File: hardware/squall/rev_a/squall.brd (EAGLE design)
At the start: 25.4 x 25.4 mm, 47 parts, among them IC1 FT232RQ, J1 MICRO_USB_B_HIROSE_ZX62R-B-5P, J2 TC2030-CTX-NL, J5 MICRO_USB_B_JST_MC5BR3-M404-4S, J6 HIROSE-DF40C-10DP-0.4V, J7 HIROSE-DF40C-10DP-0.4V, U1 FT232RL, U3 NRF51822QF, U4 LDK120PU30R, X2 16MHz

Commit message: updated squall
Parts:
- removed C1, C2, C4: 0.1u, rcl:C0603
- removed C5: 10u, SparkFun:EIA3216
- removed D2: BLUE, SparkFun:LED-0603
- removed D3: GREEN, SparkFun:LED-0603
- removed D4: RED, SparkFun:LED-0603
- removed J1: MICRO_USB_B_HIROSE_ZX62R-B-5P, connector:USB_MICRO_B-HIROSE-ZX62R-B-5P
- removed L1: (no value), SparkFun:0603
- removed R3, R4: 470, rcl:R0603
- removed U1: FT232RL, ftdichip:SSOP28
- R2: value 470 -> 12k; device rcl:R0603 -> passives:0402_RES
- moved R2 38.2 mm to (0.64, 12.7), turned to 90 degrees
- moved R8 8.91 mm to (19.1, 16.9)
- moved C18 4.64 mm to (5.21, 7.85), turned to 270 degrees
- moved C20 4.49 mm to (0.00, 19.1)
- moved U4 4.49 mm to (-0.03, 20.3)
- moved C17 4.44 mm to (11.9, 10.3), turned to 270 degrees
- moved C19 3.24 mm to (1.85, 21.8)
- moved L2 3.02 mm to (20.6, 17.6)
- moved J2 1.74 mm to (19.9, 7.09), turned to 315 degrees
- moved C3 1.51 mm to (19.8, 17.6), turned to 270 degrees
- moved L3 1.15 mm to (20.6, 15.4), turned to 270 degrees
- moved C7 0.93 mm to (17.7, 11.9)
- moved C12 0.80 mm to (17.9, 19.4)
- moved C16 0.63 mm to (13.7, 10.3)
- moved J7 0.63 mm to (3.17, 15.2), turned to 0 degrees
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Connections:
- net N$12 renamed AVDD
- net N$13 renamed DCC
- net N$28 renamed FTDI_VCC
- removed net !RST_USB: U1.3
- removed net MISO: U3.47
- removed net MOSI: U3.48
- removed net N$10: R2.1, U1.23
- removed net N$15: R3.1, U1.22
- removed net N$20: D2.C, R2.2
- removed net N$21: D3.C, R3.2
- removed net N$22: D4.C, R4.2
- removed net N$24: C16.1, J5.1, L4.1
- removed net N$25: C19.1, U4.4, U4.6
- removed net N$29: C18.1, IC1.1, IC1.16
- removed net N$8: J1.3, U1.15
- removed net N$9: C2.1, C5.A, L1.2, U1.20
- removed net RX: U1.1
- removed net SCK: U3.44
- removed net TX: U1.5
- removed net USB5V: C1.1, J1.1, L1.1
- new net 5V: C16.1, C19.1, J5.1, J7.10, J7.8, L4.1, U4.4, U4.6
- new net A5: J6.9, U3.8
- new net A6: J6.7, U3.9
- new net A7: J6.5, U3.10
- new net P08: J6.3, U3.14
- new net P09: J6.1, U3.15
- new net P10: J6.10, U3.16
- new net P11: J6.8, U3.17
- new net P12: J6.6, U3.18
- new net PROG_RX: IC1.30, U3.47
- new net PROG_TX: IC1.2, U3.48
- net 3V3: now also C18.1, IC1.1, IC1.16; no longer C4.1, D2.A, D3.A, D4.A, U1.17, U1.4
- net GND: now also BAT1.GND, J7.1, J7.9, U$2.NEG; no longer C1.2, C2.2, C4.2, C5.C, J1.5, R4.1, U1.18, U1.21, U1.25, U1.26, U1.7
- net N$1: now also R2.2, U$2.POS; no longer J1.2, U1.16
- net N$7: now also U3.19; no longer U3.15
- net SWDCLK: now also J6.2
- net SWDIO: now also J6.4
- net TCK: no longer U1.2
- net VCC: now also BAT1.POS1, BAT1.POS2, BAT1.POS3, BAT1.POS4, J7.2, J7.4, R2.1
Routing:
- net SWDCLK: track 0.00 -> 23.0 mm, vias 0 -> 2
- net SWDIO: track 0.00 -> 16.3 mm, vias 0 -> 2
- net 5V: track 0.00 -> 15.8 mm, vias 0 -> 1
- net 3V3: track 0.00 -> 12.0 mm, vias 0 -> 2
- net DCC: track 0.00 -> 11.9 mm, vias 0 -> 2
- net AVDD: track 0.00 -> 11.2 mm, vias 0 -> 2
- net P11: track 0.00 -> 10.0 mm
- net P12: track 0.00 -> 9.97 mm
- net PROG_TX: track 0.00 -> 9.70 mm, vias 0 -> 2
- net P10: track 0.00 -> 9.63 mm
- net A5: track 0.00 -> 8.33 mm
- net PROG_RX: track 0.00 -> 8.11 mm
- net N$16: track 0.00 -> 7.95 mm
- net A6: track 0.00 -> 7.87 mm
- net N$7: track 0.00 -> 7.09 mm, vias 0 -> 2
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
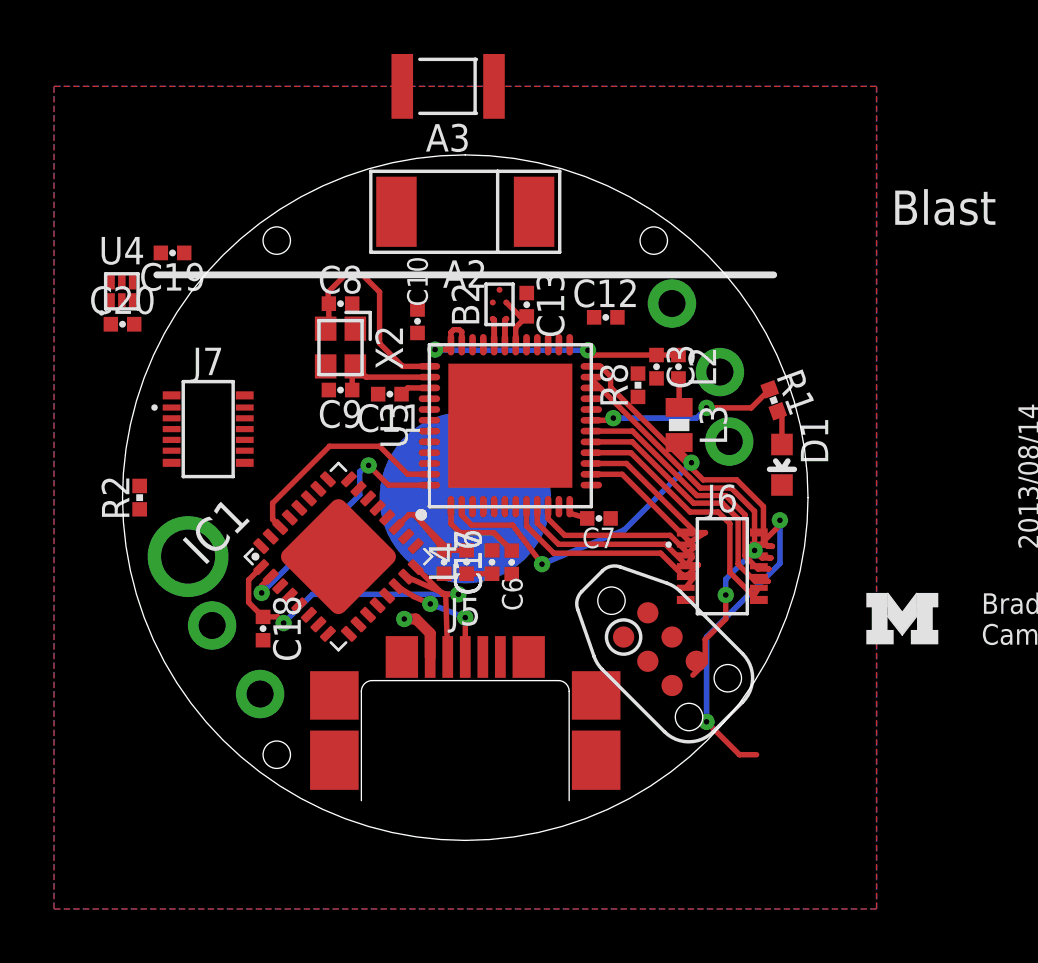
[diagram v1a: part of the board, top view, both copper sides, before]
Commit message: squall mostly routed
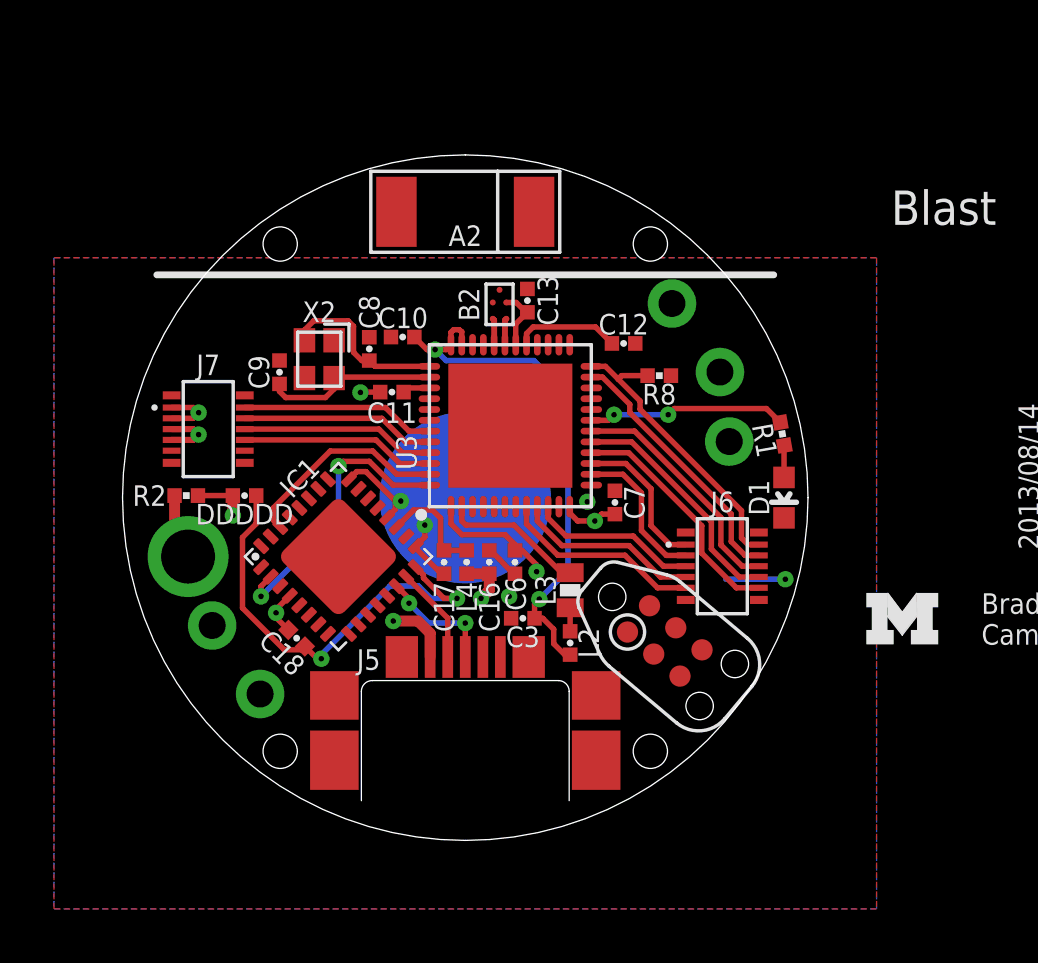
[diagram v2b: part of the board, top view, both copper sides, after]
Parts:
- removed A3: FRACTUS-2.4GHZ-FR05-S1-N-0-110, chips:FRACTUS-ANTENNA-FR05-S1-N-0-110
- removed C19, C20: 1uF, passives:0402_CAP
- removed U4: LDK120PU30R, chips:DFN6L-1.2MMX1.3MM
- added DDDDD: DIODE, passives:0402_CAP
- moved L2 11.0 mm to (16.6, 7.32), turned to 90 degrees
- moved C3 10.6 mm to (14.8, 8.23), turned to 180 degrees
- moved L3 7.33 mm to (16.6, 9.27), turned to 90 degrees
- moved C9 2.36 mm to (5.82, 17.3), turned to 90 degrees
- moved C8 1.99 mm to (9.14, 18.2), turned to 90 degrees
- moved R2 1.73 mm to (2.36, 12.8), turned to 180 degrees
- moved C18 1.29 mm to (6.45, 7.49), turned to 135 degrees
- moved R1 1.28 mm to (24.4, 15.1), turned to 280 degrees
- moved D1 1.22 mm to (24.5, 12.7)
- moved C12 1.17 mm to (18.6, 18.4)
- moved X2 0.90 mm to (7.29, 17.8)
- moved R8 0.86 mm to (19.9, 17.2), turned to 0 degrees
- moved C7 0.84 mm to (18.2, 12.5), turned to 90 degrees
- moved C10 0.80 mm to (10.4, 18.7), turned to 180 degrees
- moved J2 0.35 mm to (20.1, 7.39), turned to 320 degrees
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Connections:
- removed net N$31: C20.1, U4.1
- new net A0: J7.6, U3.45
- new net A1: J7.8, U3.46
- new net P24: J7.2, U3.43
- new net P25: J7.4, U3.44
- net 3V3: now also DDDDD.2
- net 5V: now also J7.5, J7.7; no longer C19.1, J7.10, J7.8, U4.4, U4.6
- net GND: now also J7.10; no longer C19.2, C20.2, J7.1, U4.2, U4.5
- net VCC: now also DDDDD.1, J7.1, J7.3; no longer J7.2, J7.4
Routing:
- net SWDCLK: track 23.0 -> 10.9 mm, vias 2 -> 0
- net GND: track 0.00 -> 9.39 mm, vias 0 -> 6
- net AVDD: track 11.2 -> 19.7 mm
- net P25: track 0.00 -> 7.20 mm
- net A1: track 0.00 -> 7.20 mm
- net A0: track 0.00 -> 7.20 mm
- net P24: track 0.00 -> 7.20 mm
- net VCC: track 4.21 -> 11.2 mm, vias 0 -> 4
- net DCC: track 11.9 -> 5.34 mm, vias 2 -> 0
- net 5V: track 15.8 -> 22.1 mm, vias 1 -> 3
- net 3V3: track 12.0 -> 16.7 mm
- net SWDIO: track 16.3 -> 11.9 mm, vias 2 -> 1
- net N$19: track 0.00 -> 3.93 mm
- net N$17: track 3.83 -> 6.47 mm
- net N$1: track 0.00 -> 2.47 mm
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
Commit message: squall routed
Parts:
- removed DDDDD: DIODE, passives:0402_CAP
- added C1: 0.8pF, passives:0402_CAP
- added D2: DIODE, passives:0402_DIODE
- added LOGO1: UMICH_SOLID_TINY, logos:UMICH_SOLID_50MIL
- J23: value TC2030-CTX-NL -> TC2030-JLINK-NL
- R2: value 12k -> (none)
- moved U$1 31.4 mm to (-1.70, 18.8)
- moved C12 1.41 mm to (17.5, 19.3)
- moved C13 1.32 mm to (16.3, 20.4)
- moved U3 1.27 mm to (15.6, 15.4)
- moved B2 1.27 mm to (15.2, 19.9)
- moved C7 0.93 mm to (18.9, 11.9), turned to 0 degrees
- moved R8 0.89 mm to (20.2, 18.0)
- moved C18 0.40 mm to (6.73, 7.21)
- moved L3 0.15 mm to (16.4, 9.25)
- moved A2 0.08 mm to (12.7, 23.4)
- renumbered IC1 to U2, J2 to J23, U$2 to BAT2
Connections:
- removed net !RESET: J23.3
- removed net TCK: J23.4
- removed net TDO: J23.6
- removed net TMS: J23.2
- new net P07: J6.3, U3.11
- net 3V3: now also D2.ANODE; no longer DDDDD.2
- net GND: now also C1.2
- net N$11: now also C1.1
- net P08: now also J6.1; no longer J6.3
- net P09: now also J6.10; no longer J6.1
- net P10: now also J6.8; no longer J6.10
- net P11: now also J6.6; no longer J6.8
- net P12: no longer J6.6
- net SWDCLK: now also J23.4
- net SWDIO: now also J23.2
- net VCC: now also D2.CATHODE; no longer DDDDD.1
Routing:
- net VCC: track 11.2 -> 58.2 mm, vias 4 -> 5
- net GND: track 9.39 -> 24.9 mm, vias 6 -> 30
- net P12: track 8.88 -> 0.00 mm
- net SWDIO: track 11.9 -> 18.1 mm, vias 1 -> 2
- net SWDCLK: track 10.9 -> 17.0 mm
- net P07: track 0.00 -> 4.42 mm
- net 5V: track 22.1 -> 26.4 mm
- net N$11: track 0.00 -> 2.97 mm
- net AVDD: track 19.7 -> 22.2 mm
- net N$19: track 3.93 -> 1.48 mm
- net P09: track 5.55 -> 7.68 mm
- net PROG_TX: track 10.7 -> 12.5 mm
- net DCC: track 5.34 -> 3.92 mm
- net P08: track 5.56 -> 4.25 mm
- net P25: track 7.20 -> 8.47 mm
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- removed copper zone on layer 2, net GND
- removed copper zone on layer 15, net VCC
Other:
- board size 25.4 x 25.4 mm -> 25.4 x 24 mm
- board text added: "A"
- board text added: "Squall"

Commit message: updated squall
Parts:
- removed U$1: UMICH_SOLID_SMALL, logos:UMICH_SOLID_75MIL
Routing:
- net GND: vias 30 -> 31
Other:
- board text removed: "Blast"
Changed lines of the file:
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@@
 <text x="31.8262" y="8.2042" size="0.762" layer="21" font="vector" ratio="12" align="center-left">Brad
 Campbell</text>
-<text x="30.4292" y="22.8092" size="1.27" layer="21" font="vector" ratio="14" align="bottom-center">Blast</text>
 <text x="33.9598" y="13.4874" size="0.762" layer="21" font="vector" ratio="12" rot="R90" align="bottom-center">2013/08/14</text>
 <wire x1="18.8976" y1="1.6002" x2="25.4" y2="12.7" width="0" layer="20" curve="60.85"/>
@@
 </autorouter>
 <elements>
-<element name="U$1" library="logos" package="UMICH_SOLID_75MIL" value="UMICH_SOLID_SMALL" x="-1.7018" y="18.7706"/>
 <element name="C7" library="passives" package="0402_CAP" value="0.1uF" x="18.8976" y="11.8538" smashed="yes">
 <attribute name="NAME" x="18.8976" y="11.5142" size="0.762" layer="25" font="vector" ratio="12" rot="R180" align="bottom-center"/>
@@
 <wire x1="12.1412" y1="11.0236" x2="10.3378" y2="11.0236" width="0.2032" layer="16"/>
 <contactref element="J23" pad="5"/>
+<via x="2.5654" y="18.7452" extent="1-16" drill="0.2032"/>
 </signal>
 <signal name="VCC">

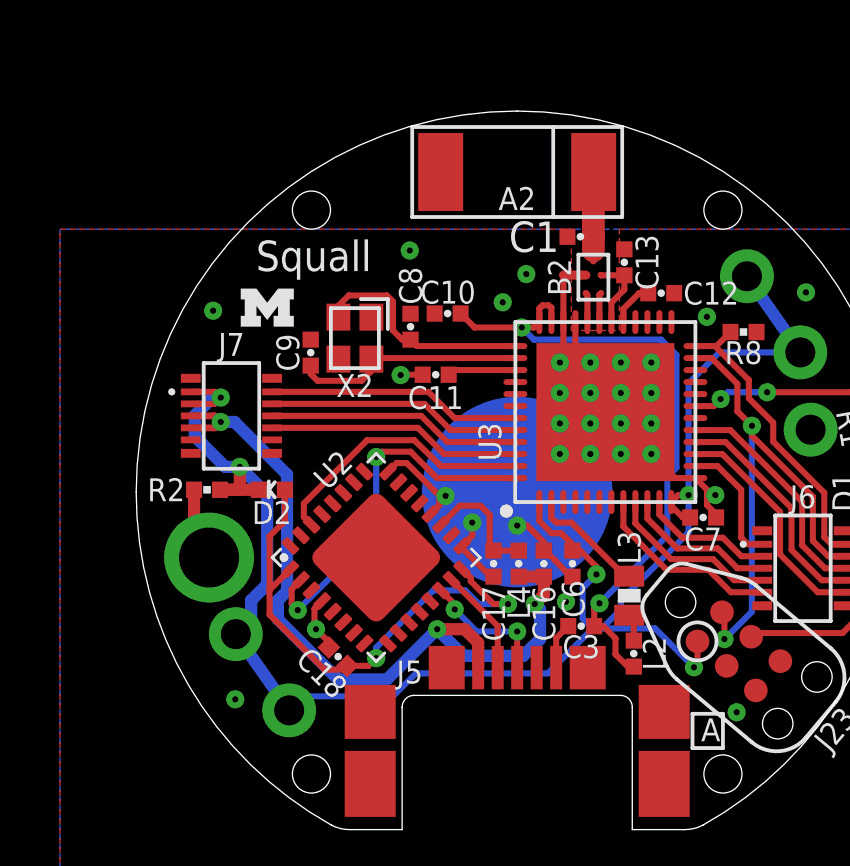
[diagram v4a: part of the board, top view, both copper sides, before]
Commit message: added 32khz crystal to squall
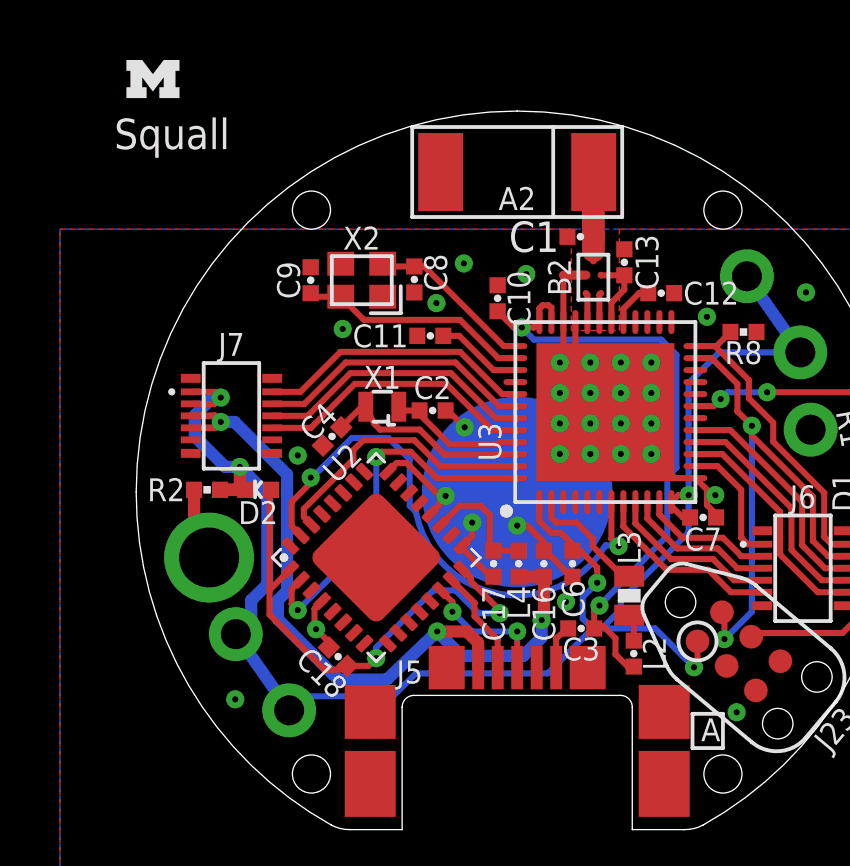
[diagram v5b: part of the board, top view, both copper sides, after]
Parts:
- added C2, C4: 12pF, passives:0402_CAP
- added X1: ABS05-32.768KHZ-9-T, crystals:ABS05
- moved LOGO1 8.52 mm to (0.56, 26.5)
- moved C9 2.41 mm to (5.82, 19.8)
- moved X2 1.94 mm to (7.52, 19.8), turned to 180 degrees
- moved C10 1.74 mm to (12.0, 19.2), turned to 90 degrees
- moved C8 1.58 mm to (9.27, 19.8), turned to 270 degrees
- moved C11 1.31 mm to (9.80, 17.9)
- moved D2 0.46 mm to (4.06, 12.8)
- moved C3 0.08 mm to (14.8, 8.15)
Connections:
- new net BTLDR_CTRL: U2.31, U3.7
- new net P21: U3.40
- new net P22: J7.2, U3.41
- new net P23: J7.4, U3.42
- net A0: now also C2.1, X1.A; no longer J7.6
- net A1: now also C4.1, X1.B; no longer J7.8
- net GND: now also C2.2, C4.2
- net P24: now also J7.6; no longer J7.2
- net P25: now also J7.8; no longer J7.4
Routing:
- net BTLDR_CTRL: track 0.00 -> 16.7 mm, vias 0 -> 2
- net P23: track 0.00 -> 9.28 mm
- net P22: track 0.00 -> 9.25 mm
- net A0: track 8.47 -> 4.50 mm
- net N$16: track 7.68 -> 5.56 mm
- net A1: track 8.47 -> 6.88 mm
- net AVDD: track 22.2 -> 21.1 mm
- net P25: track 8.47 -> 9.36 mm
- net P24: track 8.47 -> 9.32 mm
- net N$18: track 2.31 -> 2.88 mm
- net GND: track 24.9 -> 25.0 mm, vias 31 -> 32

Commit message: getting close, real close to shipping squall
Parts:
- removed C16, C17, C18: 0.1uF, passives:0402_CAP
- removed L4: (no value), passives:0402_CAP
- added C14: 1uF, passives:0402_CAP
- added C15: 4.7uF, passives:0402_CAP
- added C5: 12pF, passives:0402_CAP
- added L1: 15nH, passives:0402_CAP
- added R3: 1k, passives:0402_RES
- added S1: B3U-3000P-B, switches:B3U-3000P-B
- C10, C11: value 1nF -> 0.1uF
- C12: value 47nF -> 0.1uF
- C13: value 2.2nF -> 0.1uF
- C3: value 1uF -> 12pF
- C6: value 4.7uF -> 1nF
- C7: value 0.1uF -> 1nF
- C8: value 12pF -> 2.2nF
- C9: value 12pF -> 47nF
- L2: value (none) -> 10uH; device passives:0402_CAP -> passives:0603_CAP
- L3: value 10uH -> (none); device passives:0603_CAP -> passives:0402_CAP
- R1: value 470 -> 150
- R2: value (none) -> 150
- moved R1 19.6 mm to (5.13, 18.5), turned to 52 degrees
- moved C13 16.2 mm to (6.73, 7.21), turned to 135 degrees
- moved C9 11.7 mm to (17.5, 19.3), turned to 0 degrees
- moved C12 10.6 mm to (11.9, 10.3), turned to 270 degrees
- moved C3 10.5 mm to (6.58, 14.6), turned to 225 degrees
- moved C10 10.0 mm to (18.9, 11.9), turned to 0 degrees
- moved C7 10.0 mm to (12.0, 19.2), turned to 90 degrees
- moved C6 8.95 mm to (9.80, 17.9), turned to 180 degrees
- moved C11 8.49 mm to (13.6, 10.3), turned to 90 degrees
- moved LOGO1 8.14 mm to (7.92, 23.0)
- moved C8 7.02 mm to (16.3, 20.4), turned to 90 degrees
- moved C4 6.15 mm to (9.75, 19.8), turned to 270 degrees
- moved L3 3.83 mm to (12.8, 10.3)
- moved L2 1.94 mm to (16.4, 9.25)
- moved X2 0.46 mm to (7.98, 19.8)
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- renumbered R8 to R4
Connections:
- new net N$8: R1.2, S1.2
- net 3V3: now also C13.1; no longer C18.1
- net 5V: now also C11.1, L3.1; no longer C16.1, L4.1
- net A1: now also C3.1; no longer C4.1
- net AVDD: now also C14.1, C7.1, L1.1; no longer C10.1, C3.1, L2.1
- net DCC: now also L2.2; no longer L3.2
- net FTDI_VCC: now also C12.1, L3.2; no longer C17.1, L4.2
- net GND: now also C14.2, C15.2, C5.2, S1.1; no longer C16.2, C17.2, C18.2, D1.C
- net N$14: now also L1.2, L2.1; no longer L2.2, L3.1
- net N$16: now also C4.1; no longer C8.1
- net N$17: now also C5.1; no longer C9.1
- net N$18: now also C6.1; no longer C11.1
- net N$19: now also C9.1; no longer C12.1
- net N$23: now also R3.2; no longer R1.2
- net N$7: now also D1.C; no longer R1.1
- net SWDIO: now also R1.1
- net VCC: now also C10.1, C15.1, R3.1; no longer C6.1, C7.1
- net VDD_PA: now also C8.1; no longer C13.1
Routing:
- net SWDIO: track 18.1 -> 34.4 mm, vias 2 -> 4
- net N$7: track 6.15 -> 9.37 mm
- net N$8: track 0.00 -> 2.41 mm
- net VCC: track 57.7 -> 60.0 mm
- net GND: track 25.0 -> 26.1 mm, vias 32 -> 39
- net BTLDR_CTRL: track 16.7 -> 17.4 mm
- net N$16: track 5.56 -> 6.24 mm

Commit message: silkscreen
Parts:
- X1: value ABS05-32.768KHZ-9-T -> 16MHz; device crystals:ABS05 -> crystals:TXC-8Y
- X2: value 16MHz -> ABS05-32.768KHZ-9-T; device crystals:TXC-8Y -> crystals:ABS05
- moved X1 4.22 mm to (7.98, 19.8)
- moved X2 4.22 mm to (8.20, 15.5)
- renumbered A2 to A1, B2 to B1, J23 to J4, J5 to J3, J6 to J1, J7 to J2, U3 to U1
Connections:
- net A0: now also X2.A; no longer X1.A
- net A1: now also X2.B; no longer X1.B
- net N$16: now also X1.1; no longer X2.1
- net N$17: now also X1.3; no longer X2.3
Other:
- board text added: "2014/09/29"
- board text removed: "2013/08/14"

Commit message: squall rev a ready to ship
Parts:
- moved J1 19.7 mm to (3.17, 15.2)
- moved J2 19.7 mm to (22.2, 10.2)
- moved C1 0.25 mm to (14.6, 21.2)
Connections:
- net 5V: now also J1.5, J1.7; no longer J2.5, J2.7
- net A5: now also J2.9; no longer J1.9
- net A6: now also J2.7; no longer J1.7
- net A7: now also J2.5; no longer J1.5
- net GND: now also J1.10, J1.9; no longer J2.10, J2.9
- net P07: now also J2.3; no longer J1.3
- net P08: now also J2.1; no longer J1.1
- net P09: now also J2.10; no longer J1.10
- net P10: now also J2.8; no longer J1.8
- net P11: now also J2.6; no longer J1.6
- net P22: now also J1.2; no longer J2.2
- net P23: now also J1.4; no longer J2.4
- net P24: now also J1.6; no longer J2.6
- net P25: now also J1.8; no longer J2.8
- net SWDCLK: now also J2.2; no longer J1.2
- net SWDIO: now also J2.4; no longer J1.4
- net VCC: now also J1.1, J1.3; no longer J2.1, J2.3
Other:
- board text added: "2014/09/30"
- board text removed: "2014/09/29"
